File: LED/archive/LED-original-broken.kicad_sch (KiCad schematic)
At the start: 4 parts

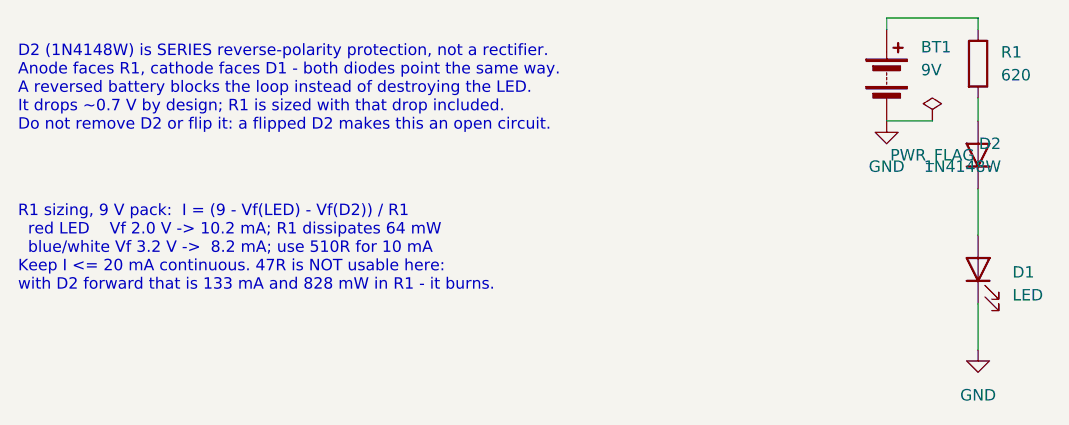
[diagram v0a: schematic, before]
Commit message: LED: promote the corrected schematic to canonical, build and route the board
- archive the broken original as archive/LED-original-broken.* (D2 reversed so
  the loop is reverse-biased, 47R at 10V = 133mA/828mW, 10V on a 1.5V cell
  symbol, no footprints on any part)
- canonical design is the former LED-revised; Device:Battery_Cell (a 1.5V cell)
  replaced by Device:Battery with a real PP3 holder; GND symbol and PWR_FLAG
  moved to the new pin-2 position so the netlist is unchanged
- footprints assigned to all four parts; D2 named 1N4148W
- on-sheet notes: D2 is load-bearing reverse-polarity protection (polarity
  matters), R1 sizing formula and the 47R failure mode documented
- LED.kicad_pcb built from an empty 78-byte stub: 66x44mm 2-layer, GND pour on
  B.Cu, one via for the LED cathode, chain parts routed in a row
- explicit DRC rules set (min track/clearance 0.2mm, via 0.6/0.3); the project
  shipped with min_clearance 0.0 / min_track_width 0.0, which made DRC vacuous
- verified: kicad-cli ERC 0 errors; DRC --schematic-parity --severity-all 0
  violations, 0 unconnected, 0 parity issues; ngspice .op 10.14mA / 64mW in R1
- README.md records the decisions, the verification and the open items (MPN and
  datasheet coverage, empty title block, gerbers not generated)
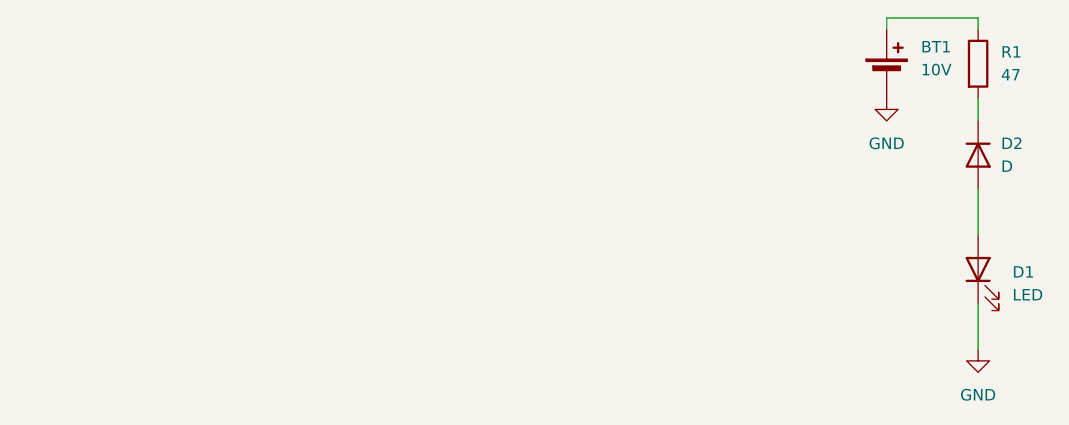
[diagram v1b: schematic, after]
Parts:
- BT1: value 9V -> 10V; footprint Battery:BatteryHolder_MPD_BA9VPC_1xPP3 -> (none); symbol Device:Battery -> Device:Battery_Cell
- D1: footprint LED_SMD:LED_0805_2012Metric -> (none)
- D2: value 1N4148W -> D; footprint Diode_SMD:D_SOD-123 -> (none)
- R1: value 620 -> 47; footprint Resistor_SMD:R_0805_2012Metric -> (none)
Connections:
- net at D1.2 (A): now also D2.2 (A); no longer D2.1 (K)
- net at R1.2: now also D2.1 (K); no longer D2.2 (A)
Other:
- note removed: "D2 (1N4148W) is SERIES reverse-polarity protection, not a rectifier. Anode faces R1, cathode faces D1 - both diodes point the same way. A reversed battery blocks the loop instead of destroying the LED. It drops ~0.7 V by design; R1 is sized with that drop included. Do not remove D2 or flip it: a flipped D2 makes this an open circuit."
- note removed: "R1 sizing, 9 V pack: I = (9 - Vf(LED) - Vf(D2)) / R1 red LED Vf 2.0 V -> 10.2 mA; R1 dissipates 64 mW blue/white Vf 3.2 V -> 8.2 mA; use 510R for 10 mA Keep I <= 20 mA continuous. 47R is NOT usable here: with D2 forward that is 133 mA and 828 mW in R1 - it burns."
- moved on the sheet: D2
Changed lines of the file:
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@@
 	)
 	(symbol
-		(lib_id "Device:Battery")
+		(lib_id "Device:Battery_Cell")
 		(at 121.92 54.61 0)
 		(unit 1)
@@
 			)
 		)
-		(property "Value" "9V"
+		(property "Value" "10V"
 			(at 125.73 54.0384 0)
 			(effects
@@
 			)
 		)
-		(property "Footprint" "Battery:BatteryHolder_MPD_BA9VPC_1xPP3"
+		(property "Footprint" ""
 			(at 121.92 53.086 90)
 			(effects
@@
 			)
 		)
-		(property "Footprint" "LED_SMD:LED_0805_2012Metric"
+		(property "Footprint" ""
 			(at 132.08 76.2 0)
 			(effects
@@
 	(symbol
 		(lib_id "power:GND")
-		(at 121.92 59.69 0)
+		(at 121.92 57.15 0)
 		(unit 1)
 		(exclude_from_sim no)
@@
 		(fields_autoplaced yes)
 		(property "Reference" "#PWR02"
-			(at 121.92 66.04 0)
+			(at 121.92 63.5 0)
 			(effects
 				(font
@@
 		)
 		(property "Value" "GND"
-			(at 121.92 64.77 0)
-			(effects
-				(font
-					(size 1.27 1.27)
-				)
-			)
-		)
-		(property "Footprint" ""
-			(at 121.92 59.69 0)
+			(at 121.92 62.23 0)
+			(effects
+				(font
+					(size 1.27 1.27)
+				)
+			)
+		)
+		(property "Footprint" ""
+			(at 121.92 57.15 0)
 			(effects
 				(font
@@
 		)
 		(property "Datasheet" ""
-			(at 121.92 59.69 0)
+			(at 121.92 57.15 0)
 			(effects
 				(font
@@
 		)
 		(property "Description" "Power symbol creates a global label with name \"GND\" , ground"
-			(at 121.92 59.69 0)
+			(at 121.92 57.15 0)
 			(effects
 				(font
@@
 			)
 		)
-		(property "Value" "620"
+		(property "Value" "47"
 			(at 134.62 54.6099 0)
 			(effects
@@
 			)
 		)
-		(property "Footprint" "Resistor_SMD:R_0805_2012Metric"
+		(property "Footprint" ""
 			(at 130.302 53.34 90)
 			(effects
@@
 	(symbol
 		(lib_id "Device:D")
-		(at 132.08 63.5 90)
+		(at 132.08 63.5 270)
 		(unit 1)
 		(exclude_from_sim no)
@@
 			)
 		)
-		(property "Value" "1N4148W"
+		(property "Value" "D"
 			(at 134.62 64.7699 90)
 			(effects
@@
 			)
 		)
-		(property "Footprint" "Diode_SMD:D_SOD-123"
+		(property "Footprint" ""
 			(at 132.08 63.5 0)
 			(effects
@@
 		)
 	)
-	(wire
-		(pts
-			(xy 121.92 59.69)
-			(xy 127 59.69)
-		)
-		(stroke
-			(width 0)
-			(type default)
-		)
-	)
-	(symbol
-		(lib_id "power:PWR_FLAG")
-		(at 127 59.69 0)
-		(unit 1)
-		(exclude_from_sim no)
-		(in_bom yes)
-		(on_board yes)
-		(dnp no)
-		(fields_autoplaced yes)
-		(property "Reference" "#FLG01"
-			(at 127 57.15 0)
-			(effects
-				(font
-					(size 1.27 1.27)
-				)
-				(hide yes)
-			)
-		)
-		(property "Value" "PWR_FLAG"
-			(at 127 63.5 0)
-			(effects
-				(font
-					(size 1.27 1.27)
-				)
-			)
-		)
-		(property "Footprint" ""
-			(at 127 59.69 0)
-			(effects
-				(font
-					(size 1.27 1.27)
-				)
-				(hide yes)
-			)
-		)
-		(property "Datasheet" ""
-			(at 127 59.69 0)
-			(effects
-				(font
-					(size 1.27 1.27)
-				)
-				(hide yes)
-			)
-		)
-		(property "Description" "Special symbol for telling ERC where power comes from"
-			(at 127 59.69 0)
-			(effects
-				(font
-					(size 1.27 1.27)
-				)
-				(hide yes)
-			)
-		)
-		(pin "1"
-		)
-		(instances
-			(project ""
-				(path "/1871d796-7bb9-43f9-8079-125c20ef5a39"
-					(reference "#FLG01")
-					(unit 1)
-				)
-			)
-		)
-	)
-	(text "D2 (1N4148W) is SERIES reverse-polarity protection, not a rectifier.\nAnode faces R1, cathode faces D1 - both diodes point the same way.\nA reversed battery blocks the loop instead of destroying the LED.\nIt drops ~0.7 V by design; R1 is sized with that drop included.\nDo not remove D2 or flip it: a flipped D2 makes this an open circuit."
-		(exclude_from_sim no)
-		(at 25.4 60.96 0)
-		(effects
-			(font
-				(size 1.27 1.27)
-			)
-			(justify left bottom)
-		)
-	)
-	(text "R1 sizing, 9 V pack:  I = (9 - Vf(LED) - Vf(D2)) / R1\n  red LED    Vf 2.0 V -> 10.2 mA; R1 dissipates 64 mW\n  blue/white Vf 3.2 V ->  8.2 mA; use 510R for 10 mA\nKeep I <= 20 mA continuous. 47R is NOT usable here:\nwith D2 forward that is 133 mA and 828 mW in R1 - it burns."
-		(exclude_from_sim no)
-		(at 25.4 78.74 0)
-		(effects
-			(font
-				(size 1.27 1.27)
-			)
-			(justify left bottom)
-		)
-	)
